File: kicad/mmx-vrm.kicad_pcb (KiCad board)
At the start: 2 copper layers, 39.8 x 43.9 mm, 18 parts, among them J1 Conn_02x15_Row_Letter_First, SW1 SW_DIP_x03, U1 LM2596S, U2 LM2596S

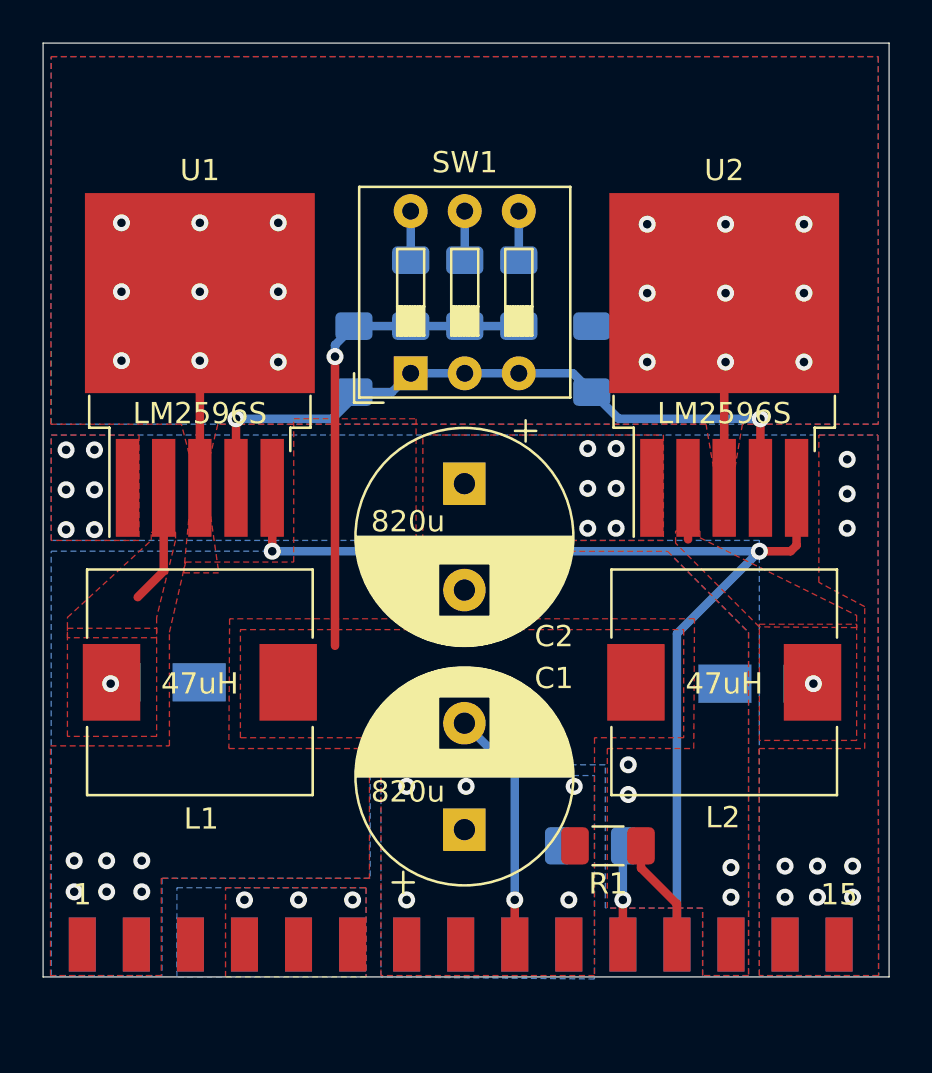
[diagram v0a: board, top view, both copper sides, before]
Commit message: Minor layout improvements
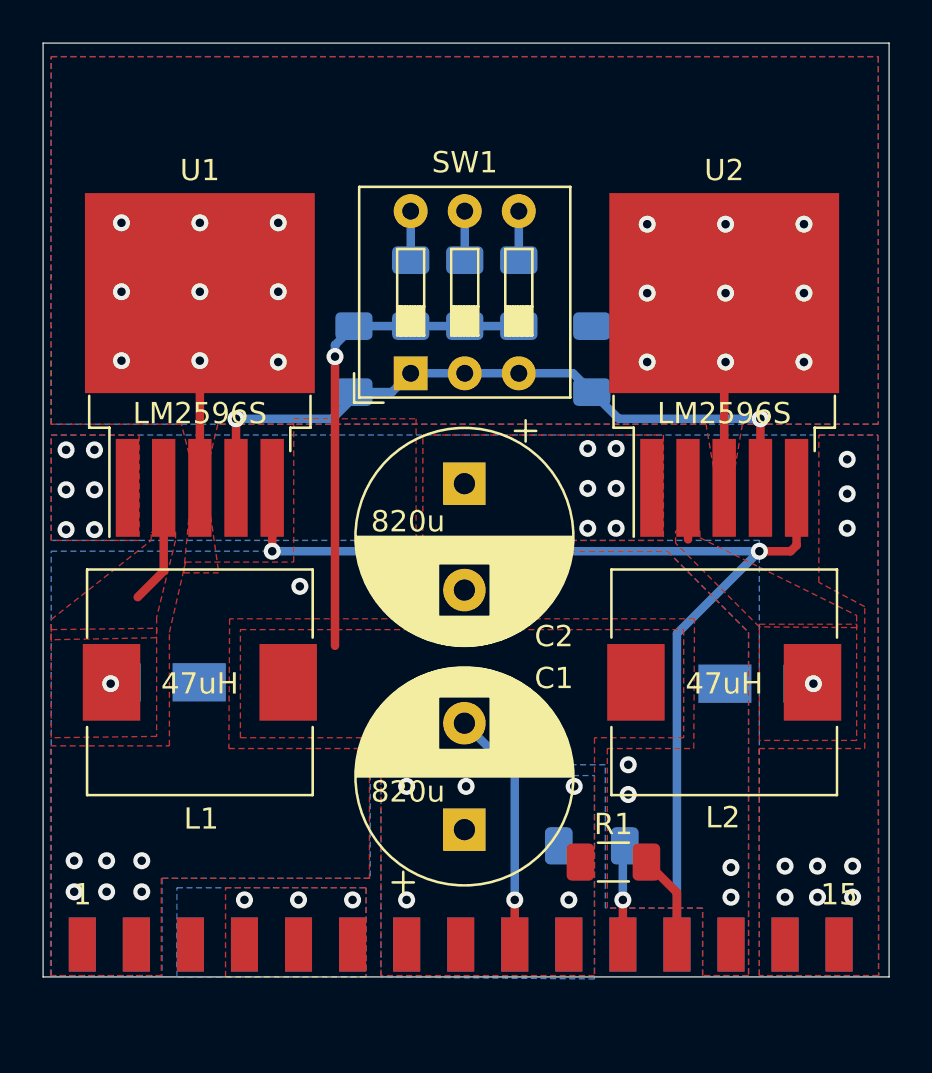
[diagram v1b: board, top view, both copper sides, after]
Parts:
- moved R1 0.80 mm to (139.4, 97.5)
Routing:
- net SENSE: track 5.33 -> 4.47 mm
- net GND: vias 29 -> 31

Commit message: Improve clearance, rev 0.3 started
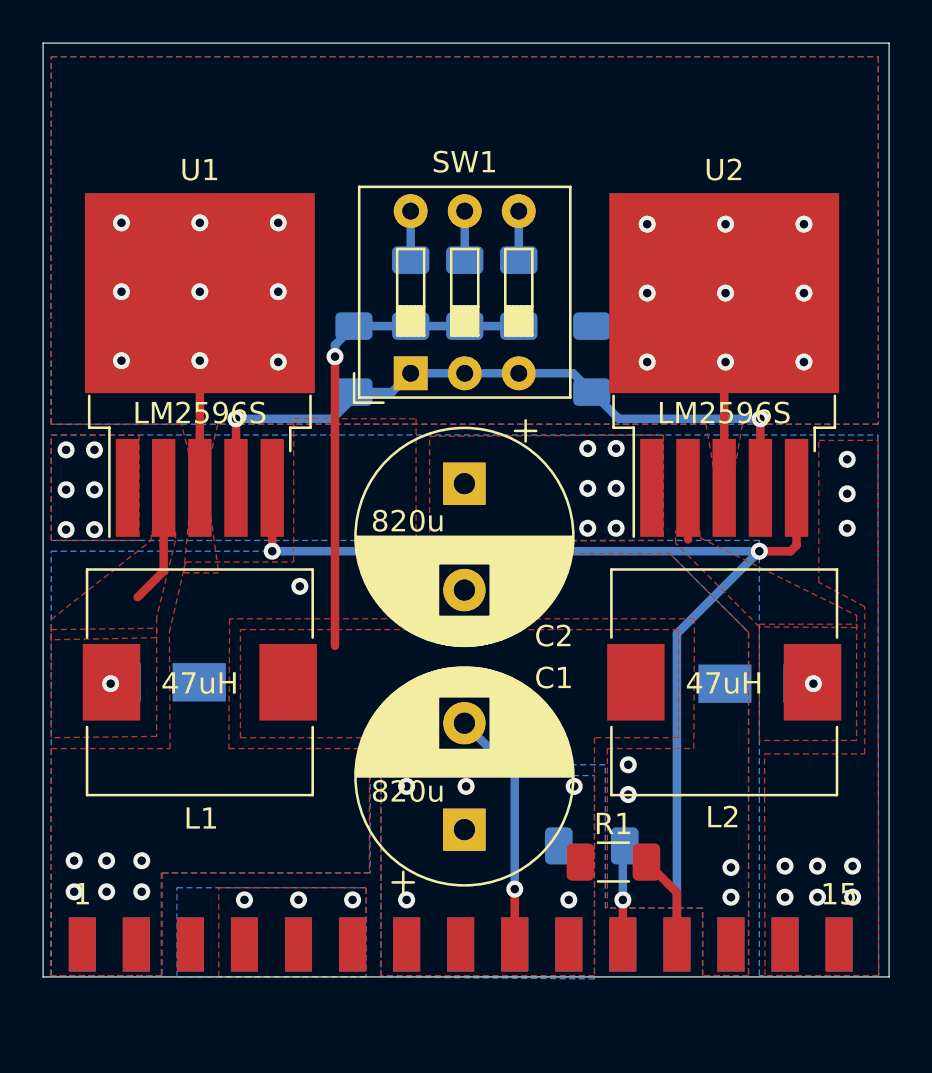
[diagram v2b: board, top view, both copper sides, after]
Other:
- board text added: "rev 0.2"
- board text removed: "rev 0.1"
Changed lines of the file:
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@@
   (title_block
     (title MMX-VRM)
-    (date 2021-08-22)
-    (rev 0.1)
+    (date 2021-09-06)
+    (rev 0.2)
     (company Necroware)
     (comment 1 "by Scorp")
@@
     (last_trace_width 0.4)
     (trace_clearance 0.2)
-    (zone_clearance 0.254)
+    (zone_clearance 0.508)
     (zone_45_only no)
     (trace_min 0.2)
@@
     (effects (font (size 1 1) (thickness 0.2)) (justify left mirror))
   )
-  (gr_text "rev 0.1" (at 120.142 95.25) (layer B.SilkS)
+  (gr_text "rev 0.2" (at 120.142 95.25) (layer B.SilkS)
     (effects (font (size 1.5 1.5) (thickness 0.3)) (justify mirror))
   )
@@
   (segment (start 144.653 73.8505) (end 144.7165 73.787) (width 0.4) (layer F.Cu) (net 1))
   (segment (start 144.653 79.9525) (end 144.653 74.1045) (width 0.4) (layer F.Cu) (net 1))
-  (segment (start 134.8105 99.314) (end 134.8105 101.4095) (width 0.4) (layer F.Cu) (net 1))
-  (via micro (at 134.8105 99.314) (size 0.8) (drill 0.4) (layers F.Cu B.Cu) (net 1))
-  (segment (start 134.8105 93.3765) (end 132.446 91.012) (width 0.4) (layer B.Cu) (net 1))
-  (segment (start 134.8105 99.314) (end 134.8105 93.3765) (width 0.4) (layer B.Cu) (net 1))
   (via micro (at 128.524 84.582) (size 0.8) (drill 0.4) (layers F.Cu B.Cu) (net 1))
   (via micro (at 124.714 84.582) (size 0.8) (drill 0.4) (layers F.Cu B.Cu) (net 1))
+  (via micro (at 134.8105 98.805998) (size 0.8) (drill 0.4) (layers F.Cu B.Cu) (net 1))
+  (segment (start 134.8105 101.4095) (end 134.8105 98.805998) (width 0.4) (layer F.Cu) (net 1))
+  (segment (start 132.446 91.012) (end 134.8105 93.3765) (width 0.4) (layer B.Cu) (net 1))
+  (segment (start 134.8105 93.3765) (end 134.8105 98.805998) (width 0.4) (layer B.Cu) (net 1))
   (via micro (at 150.4315 81.8515) (size 0.8) (drill 0.4) (layers F.Cu B.Cu) (net 2))
   (via micro (at 150.4315 78.613) (size 0.8) (drill 0.4) (layers F.Cu B.Cu) (net 2))
@@
   (segment (start 129.921 69.2525) (end 129.921 66.95) (width 0.4) (layer B.Cu) (net 13))
   (zone (net 5) (net_name +3.3V) (layer B.Cu) (hatch edge 0.508)
-    (connect_pads (clearance 0.254))
+    (connect_pads (clearance 0.508))
     (min_thickness 0.254)
     (fill yes (arc_segments 32) (thermal_gap 0.254) (thermal_bridge_width 0.508))
@@
   )
   (zone (net 5) (net_name +3.3V) (layer F.Cu) (hatch edge 0.508)
-    (connect_pads (clearance 0.254))
+    (connect_pads (clearance 0.508))
     (min_thickness 0.254)
     (fill yes (arc_segments 32) (thermal_gap 0.254) (thermal_bridge_width 0.508))
     (polygon
       (pts
-        (xy 127.8255 102.9335) (xy 121.2215 102.9335) (xy 121.2215 98.7425) (xy 127.8255 98.7425)
+        (xy 127.8255 102.9335) (xy 120.904 102.9335) (xy 120.904 98.7425) (xy 127.8255 98.7425)
       )
     )
@@
   )
   (zone (net 2) (net_name +5V) (layer B.Cu) (hatch edge 0.508)
-    (connect_pads (clearance 0.254))
+    (connect_pads (clearance 0.508))
     (min_thickness 0.254)
     (fill yes (arc_segments 32) (thermal_gap 0.254) (thermal_bridge_width 0.508))
@@
     (polygon
       (pts
-        (xy 151.905247 102.870003) (xy 146.304 102.870037) (xy 146.282977 92.201974) (xy 151.257 92.202026) (xy 151.257 85.5345)
-        (xy 149.098 84.3915) (xy 149.098 77.47) (xy 151.878753 77.469998)
+        (xy 151.905247 102.870003) (xy 146.568512 102.870032) (xy 146.547739 92.455972) (xy 151.256749 92.456029) (xy 151.257 85.5345)
+        (xy 149.098 84.3915) (xy 149.098 77.724001) (xy 151.878753 77.723999)
       )
     )
   )
   (zone (net 2) (net_name +5V) (layer F.Cu) (hatch edge 0.508)
-    (connect_pads thru_hole_only (clearance 0.254))
+    (connect_pads thru_hole_only (clearance 0.508))
     (min_thickness 0.254)
-    (fill yes (arc_segments 32) (thermal_gap 0.508) (thermal_bridge_width 0.508))
+    (fill yes (arc_segments 32) (thermal_gap 0.254) (thermal_bridge_width 0.508))
     (polygon
       (pts
-        (xy 141.7955 82.423) (xy 130.4925 82.423) (xy 130.4925 77.47) (xy 141.7955 77.47)
+        (xy 141.7955 82.423) (xy 130.81 82.4865) (xy 130.81 77.5335) (xy 141.7955 77.47)
       )
     )
@@
   )
   (zone (net 3) (net_name VCORE) (layer F.Cu) (hatch edge 0.508)
-    (connect_pads (clearance 0.254))
+    (connect_pads (clearance 0.508))
     (min_thickness 0.254)
     (fill yes (arc_segments 32) (thermal_gap 0.254) (thermal_bridge_width 0.508))
     (polygon
       (pts
-        (xy 142.748 91.694) (xy 138.557 91.694) (xy 138.557 102.87) (xy 128.524 102.87) (xy 128.524 91.694)
-        (xy 121.92 91.694) (xy 121.92 86.614) (xy 142.748 86.614)
+        (xy 142.494 91.694) (xy 138.557 91.694) (xy 138.557 102.87) (xy 128.524 102.87) (xy 128.524 91.694)
+        (xy 121.92 91.694) (xy 121.92 86.614) (xy 142.494 86.614)
       )
     )
   )
   (zone (net 1) (net_name GND) (layer F.Cu) (hatch edge 0.508)
-    (connect_pads thru_hole_only (clearance 0.254))
+    (connect_pads thru_hole_only (clearance 0.508))
     (min_thickness 0.254)
     (fill yes (arc_segments 32) (thermal_gap 0.254) (thermal_bridge_width 0.508))
@@
   )
   (zone (net 1) (net_name GND) (layer B.Cu) (hatch edge 0.508)
-    (connect_pads (clearance 0.254))
+    (connect_pads (clearance 0.508))
     (min_thickness 0.254)
     (fill yes (arc_segments 32) (thermal_gap 0.254) (thermal_bridge_width 0.508))
@@
       (pts
         (xy 145.796 86.741) (xy 145.796 102.87) (xy 143.637 102.87) (xy 143.637 99.695) (xy 139.065 99.695)
-        (xy 139.065 92.964) (xy 128.016 92.964) (xy 128.016 98.298) (xy 118.237 98.298) (xy 118.237 102.87)
+        (xy 139.065 92.964) (xy 128.016 92.964) (xy 128.016 98.044) (xy 118.237 98.044) (xy 118.237 102.87)
         (xy 113.03 102.87) (xy 113.03 82.931) (xy 141.986 82.931)
       )
@@
   )
   (zone (net 1) (net_name GND) (layer B.Cu) (hatch edge 0.508)
-    (connect_pads (clearance 0.254))
+    (connect_pads (clearance 0.508))
     (min_thickness 0.254)
     (fill yes (arc_segments 32) (thermal_gap 0.254) (thermal_bridge_width 0.508))
@@
   )
   (zone (net 1) (net_name GND) (layer F.Cu) (hatch edge 0.508)
-    (connect_pads (clearance 0.254))
+    (connect_pads (clearance 0.508))
     (min_thickness 0.254)
     (fill yes (arc_segments 32) (thermal_gap 0.254) (thermal_bridge_width 0.508))
@@
         (xy 145.796 86.741) (xy 145.796 102.87) (xy 143.637 102.87) (xy 143.637 99.695) (xy 139.158005 99.695)
         (xy 139.158005 92.202) (xy 143.222005 92.202) (xy 143.256 86.106) (xy 121.412 86.106) (xy 121.378005 92.202)
-        (xy 127.982005 92.202) (xy 127.982005 98.298) (xy 118.203005 98.298) (xy 118.203005 102.87) (xy 112.996005 102.87)
-        (xy 112.996005 92.075) (xy 118.584005 92.075) (xy 118.584005 86.741) (xy 119.346005 83.439) (xy 124.426005 83.439)
-        (xy 124.426005 76.708) (xy 130.175 76.708) (xy 130.175 82.931) (xy 141.986 82.931)
+        (xy 127.982005 92.202) (xy 127.982005 98.044) (xy 118.203005 98.044) (xy 118.203005 102.87) (xy 112.996005 102.87)
+        (xy 113.03 92.202) (xy 118.618 92.202) (xy 118.584005 86.741) (xy 119.346005 83.439) (xy 124.426005 83.439)
+        (xy 124.426005 76.708) (xy 130.175 76.708) (xy 130.175 83.058) (xy 142.113 83.058)
       )
     )

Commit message: Fixes after first tests
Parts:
- added C3: 10nF, Capacitor_SMD:C_1206_3216Metric_Pad1.33x1.80mm_HandSolder, B.Cu at (124.7, 73.9)
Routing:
- net VCORE: track 23.1 -> 27.6 mm
- net Net-(D2-Pad1): track 4.46 -> 6.38 mm
- net GND: track 23.4 -> 24.4 mm, vias 31 -> 35
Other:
- board size 39.8 x 43.9 mm -> 39.8 x 46.4 mm

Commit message: Readjusted the resistors for 3.2V support
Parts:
- R3: value 15K -> 9K
- R4: value 7.5K -> 6.3K
- R5: value 3K -> 2.9K
- R6: value 1.5K -> 1.6K
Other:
- board text added: "SW1 Settings: 000: 3.2V 100: 2.9V 010: 2.8V 110: 2.6V 001: 2.5V 101: 2.4V 011: 2.3V 111: 2.2V"
- board text removed: "SW1 Settings: 000: 3.0V 100: 2.9V 010: 2.8V 110: 2.6V 001: 2.5V 101: 2.4V 011: 2.3V 111: 2.2V"
